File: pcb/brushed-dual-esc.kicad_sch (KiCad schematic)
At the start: 31 parts, among them J2 TC2030-NL, J3 DRV1_OUT1, J4 Conn_01x04_Pin, J5 DRV1_OUT2, J6 DRV2_OUT1, J7 DRV2_OUT2, J8 +BATT, J9 -BATT, U1 AZ1117CR-5.0TRG1, U2 TLV77133PDBVR, U3 STM32C011F6U6, U6 DRV8231ADDAR, U7 DRV8231ADDAR

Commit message: Begin routing
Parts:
- removed J4: Conn_01x04_Pin, Connector_PinHeader_2.54mm:PinHeader_1x04_P2.54mm_Vertical, symbol Connector:Conn_01x04_Pin
- added J10: RX_CH2, Connector_Wire:SolderWirePad_1x01_SMD_1x2mm, symbol Connector_Generic:Conn_01x01
- added J11: RX_CH1, Connector_Wire:SolderWirePad_1x01_SMD_1x2mm, symbol Connector_Generic:Conn_01x01
- added J12: +5V, Connector_Wire:SolderWirePad_1x01_SMD_1x2mm, symbol Connector_Generic:Conn_01x01
- added J13: GND, Connector_Wire:SolderWirePad_1x01_SMD_1x2mm, symbol Connector_Generic:Conn_01x01
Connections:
- net +5V: now also J12.1 (Pin_1)
- net BATT_SENSE: now also U3.5 (PA0); no longer U3.15 (PA10/PA12)
- net DRV1_IN1: now also U3.13 (PA8); no longer U3.6 (PA1)
- net DRV1_IN2: now also U3.14 (PA9/PA11); no longer U3.7 (PA2)
- net DRV1_ISENSE: now also U3.15 (PA10/PA12); no longer U3.5 (PA0)
- net DRV2_IN1: now also U3.6 (PA1); no longer U3.14 (PA9/PA11)
- net DRV2_IN2: now also U3.7 (PA2); no longer U3.13 (PA8)
- net GND: now also J13.1 (Pin_1)
- net RX_CH1: now also J11.1 (Pin_1)
- net RX_CH2: now also J10.1 (Pin_1)

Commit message: Prep for BOM
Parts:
- C1: value CL31A226KAHNNNE -> 10µF 25V; footprint Capacitor_SMD:C_1206_3216Metric -> Capacitor_SMD:C_0805_2012Metric; MPN (none) -> GRM21BR61E106MA73L
- C10, C11: value A768EB107M1ELAS036 -> 100uF 25V; MPN (none) -> A768EB107M1ELAS036
- C2, C4, C5: value 4.7u -> 4.7u 10V; MPN (none) -> GMC10X5R475K10NT
- C3: value CL31A226KAHNNNE -> 22uF 10V; footprint Capacitor_SMD:C_1206_3216Metric -> Capacitor_SMD:C_0603_1608Metric; MPN (none) -> GRM188R61A226ME15D
- C6, C8, C9: value 100n -> 100n 50V; MPN (none) -> 885012206095R
- D2: value B1911USD -> Vf=1.9V; MPN (none) -> LC19DJECT-2MA-U1
- J10, J11, J12, J13, J3, J5, J6, J7, J8, J9: now left out of the parts list
- R2: value 47k -> 33k; MPN (none) -> RT0603FRE1033KL
- R3: MPN (none) -> RNCP0603FTD10K0
- R4, R5: MPN (none) -> RNCP0603FTD750R
- R6: value 270 -> 750; MPN (none) -> RNCP0603FTD750R
- U1: MPN (none) -> AZ1117CR-5.0TRG1
- U2: MPN (none) -> TLV77133PDBVR
- U3: MPN (none) -> STM32C011F6U6
- U6, U7: MPN (none) -> DRV8231ADDAR
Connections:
- net +3V3: no longer R6.1
- net +5V: now also R6.1
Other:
- moved on the sheet: C8, C9

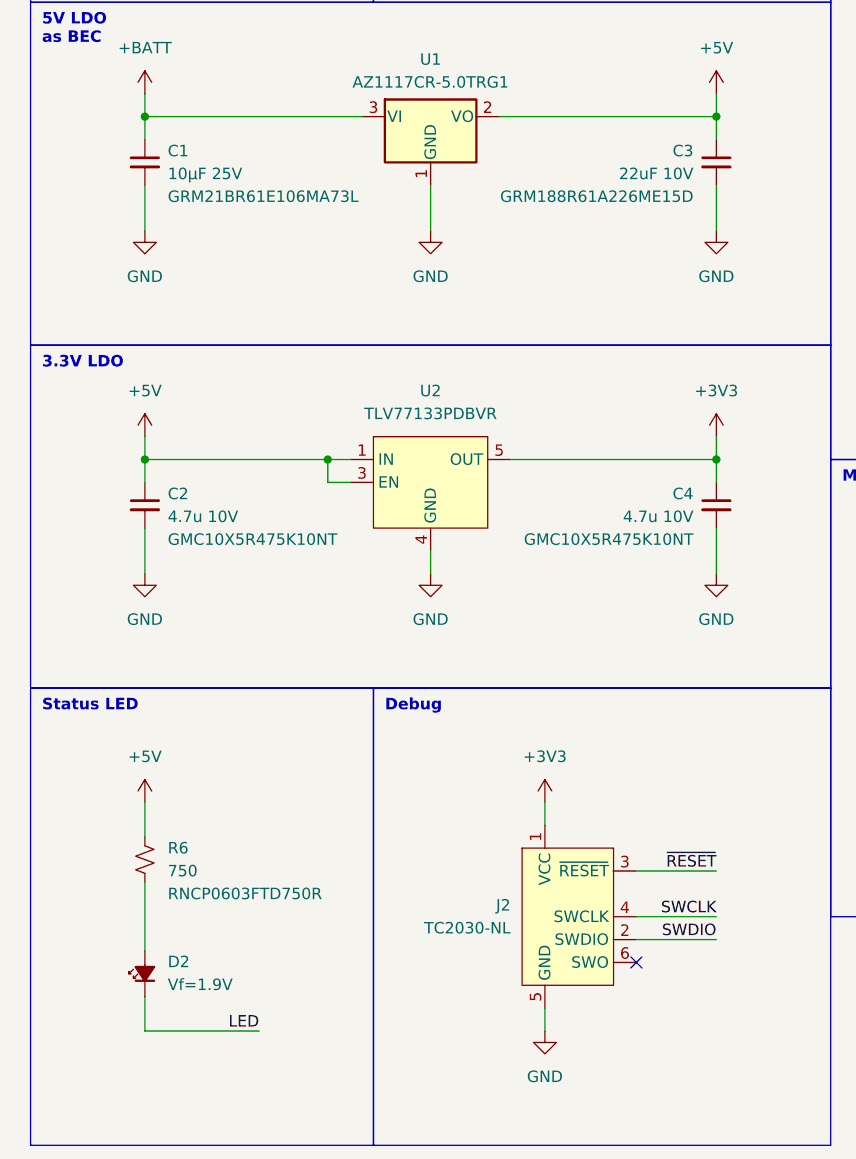
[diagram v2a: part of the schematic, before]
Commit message: Cleanup BOM and generate PnP
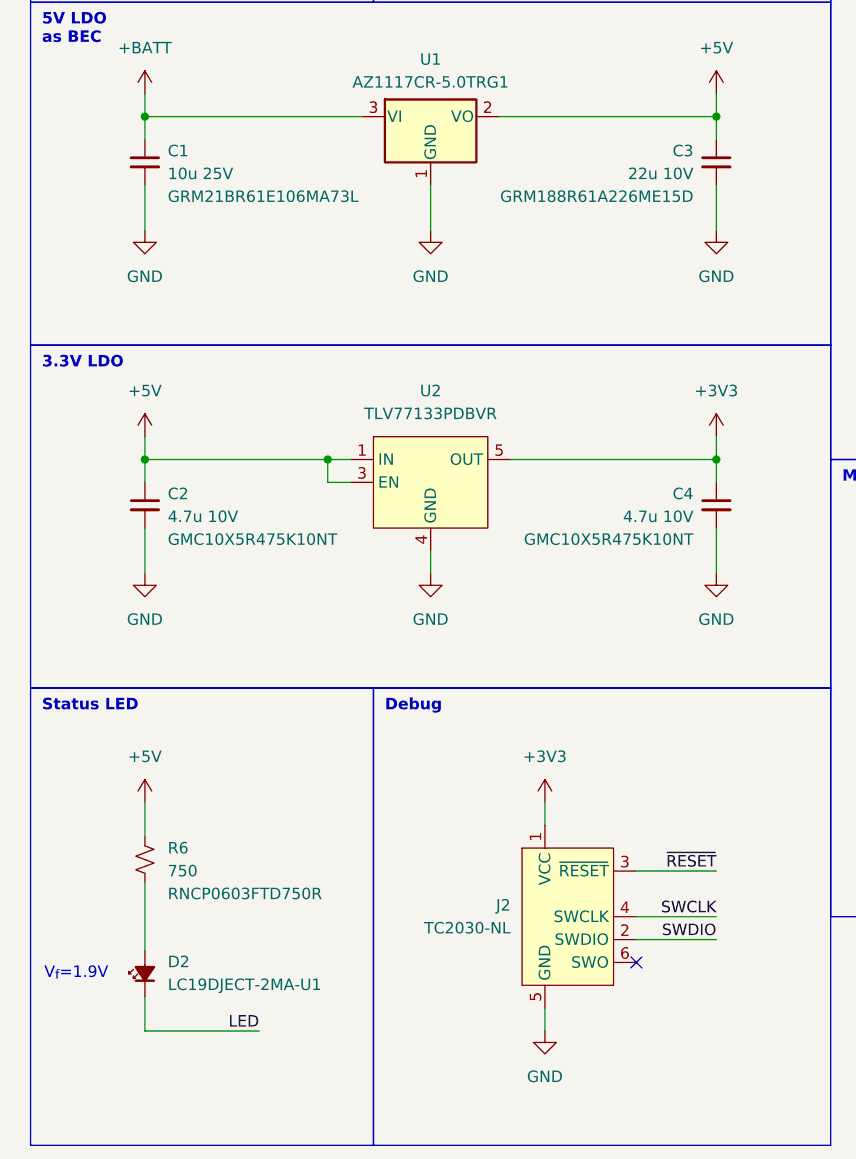
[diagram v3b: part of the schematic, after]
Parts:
- C1: value 10µF 25V -> 10u 25V
- C3: value 22uF 10V -> 22u 10V
- D2: value Vf=1.9V -> LC19DJECT-2MA-U1
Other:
- note added: "V_{f}=1.9V"
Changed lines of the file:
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@@
 		)
 	)
+	(text "V_{f}=1.9V"
+		(exclude_from_sim no)
+		(at 17.78 171.45 0)
+		(effects
+			(font
+				(size 1.27 1.27)
+			)
+		)
+	)
 	(text "Battery connection"
 		(exclude_from_sim no)
@@
 			)
 		)
-		(property "Value" "22uF 10V"
+		(property "Value" "22u 10V"
 			(at 86.36 82.5562 0)
 			(show_name no)
@@
 			)
 		)
-		(property "Value" "10µF 25V"
+		(property "Value" "10u 25V"
 			(at 27.94 82.5562 0)
 			(show_name no)
@@
 			)
 		)
-		(property "Value" "Vf=1.9V"
+		(property "Value" "LC19DJECT-2MA-U1"
 			(at 27.94 172.6564 90)
 			(show_name no)
